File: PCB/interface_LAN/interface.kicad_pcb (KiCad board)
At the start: 4 copper layers, 100 x 75 mm, 167 parts, among them J1 24VAC, J10 LIMIT12, J11 POT, J12 RS485, J4 Power, J5 Control Signals, J6 HR913550A, J7 Sensor Feedback, J8 UART, J9 POT, Q1 8550, Q2 TIP127, Q3 MMBT5551, SW1 SW_SPST, SW2 CW, SW3 CCW, SW4 SET, U1 B1205-1W, U10 EL357, U11 74HCT595, U12 EL357, U13 AT24C64, U14 TL072, U15 HCNR201, U17 LMV358, U18 EL357, U19 EL357, U2 ESP32-WROOM-32, U20 EL357, U21 MAX485E, U22 TPS54160, U3 LM317_TO-220, U4 L78L05_SOT89, U5 AMS1117-3.3, U6 OLED_128x32_4pin, U7 LAN8720A, U9 HCNR201

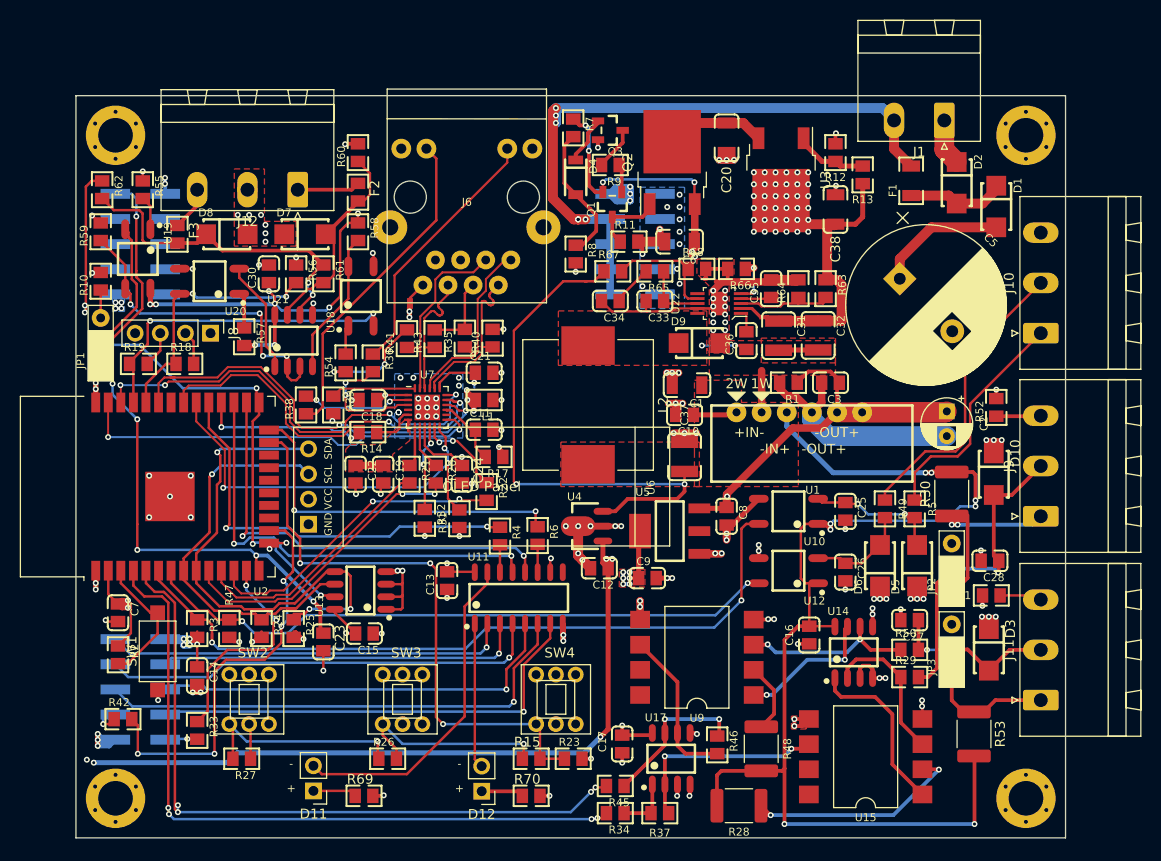
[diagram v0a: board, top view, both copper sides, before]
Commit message: Routed Interface_LAN MCU board
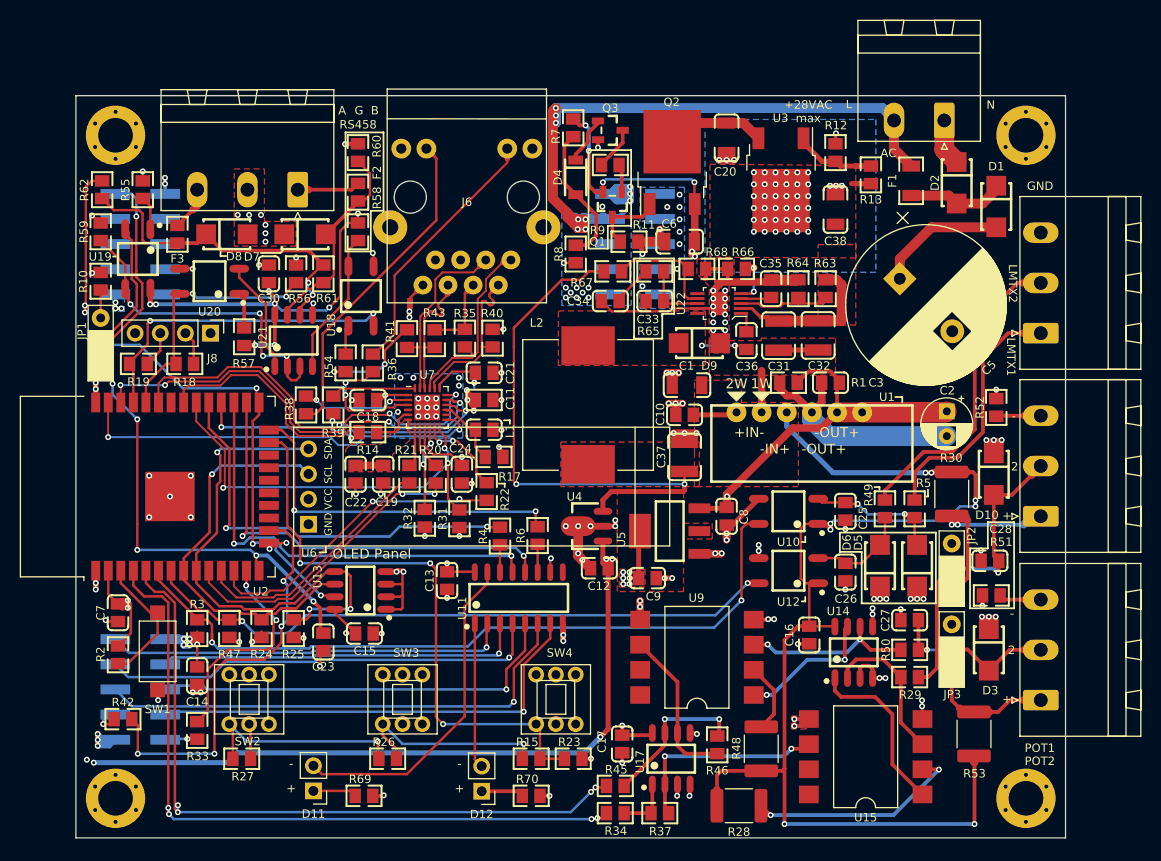
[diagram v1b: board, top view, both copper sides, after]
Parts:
- moved R13 0.83 mm to (100.3, 28.0)
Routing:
- net /+24V: track 31.4 -> 14.8 mm
- net GNDPWR: track 129.7 -> 134.8 mm, vias 86 -> 87
- net Net-(J11-Pad1): track 10.2 -> 14.8 mm
- net Net-(J9-Pad1): track 20.3 -> 23.1 mm
- net Net-(J10-Pad1): track 23.7 -> 25.7 mm
- net Net-(R12-Pad1): track 7.33 -> 8.92 mm
- net VAC: track 71.4 -> 72.9 mm, vias 6 -> 16
- net Net-(J10-Pad2): track 30.3 -> 31.6 mm
- net GND: track 104.7 -> 105.8 mm, vias 68 -> 66
- net /SDA: track 52.2 -> 52.8 mm
- net +12V: track 214.1 -> 214.7 mm
- added copper zone on B.Cu, net /+24V
- added copper zone on F.Cu, net /+24V
- added copper zone on B.Cu, net VAC
- added copper zone on In2.Cu, net VAC
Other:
- board text added: "+28VAC max"
- board text added: "2"
- board text added: "A"
- board text added: "AC"
- board text added: "B"
- board text added: "G"
- board text added: "GND"
- board text added: "L"
- board text added: "LMTX1"
- board text added: "LMTX2"
- board text added: "N"
- board text added: "POT1"
- board text added: "POT2"
- board text added: "RS458"

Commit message: Implemented the ESP-IDF version. First passed compilation
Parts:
- added C29: 104, lc_lib:0805_C, F.Cu at (62.1, 83.5)
- added C39: 104, lc_lib:0805_C, F.Cu at (70.2, 89.7)
- added C4: 1000uF 63V, Connector_JST:JST_XH_B2B-XH-A_1x02_P2.50mm_Vertical, F.Cu at (105.0, 40.3)
- added C40: 104, lc_lib:0805_C, F.Cu at (70.2, 92.5)
- added J2: 0, lc_lib:1206_R, F.Cu at (89.2, 26.2)
- added J3: JTAG, Connector_PinHeader_2.54mm:PinHeader_1x04_P2.54mm_Vertical, F.Cu at (48.8, 90.3)
- R3: value 4.7K -> 100K
- R9: value 47K -> 10K
- U7: footprint Package_DFN_QFN:QFN-24-1EP_4x4mm_P0.5mm_EP2.6x2.6mm -> lc_lib:QFN-24_4X4X05P
- moved R3 25.3 mm to (57.5, 73.8)
- moved R47 18.2 mm to (53.7, 74.4), turned to 180 degrees
- moved R69 9.71 mm to (44.0, 82.5), turned to 90 degrees
- moved C23 9.49 mm to (35.6, 73.9)
- turned U7 to 270 degrees
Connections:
- net /SPWM1 renamed /SPWM1_TCK
- net /SPWM2 renamed /SPWM2_TMS
- D11 pad 2: /LEDAX -> /LEDAX_485RW
- J8 pad 2: /PROG_TXD -> /PROG_RXD
- J8 pad 3: /PROG_RXD -> /PROG_TXD
- JP1 pad 2: /BOOT_WP_485RW -> /BOOT_WP
- R18 pad 2: /PROG_TXD -> /PROG_RXD
- R19 pad 2: /PROG_RXD -> /PROG_TXD
- R3 pad 1: /LMTX1 -> /LMTX2_TDO
- R3 pad 2: +3V3 -> GND
- R47 pad 2: /LMTX2 -> /LMTX2_TDO
- U10 pad 4: /LMTX1 -> /LMTX1_TDI
- U11 pad 15: /LEDAX -> /LEDAX_485RW
- U12 pad 4: /LMTX2 -> /LMTX2_TDO
- U13 pad 7: /BOOT_WP_485RW -> /BOOT_WP
- U19 pad 2: /BOOT_WP_485RW -> /LEDAX_485RW
- U2 pad 14: /ISense1 -> /LMTX1_TDI
- U2 pad 23: /ADC_Manual -> /LMTX2_TDO
- U2 pad 25: /BOOT_WP_485RW -> /BOOT_WP
- U2 pad 4: /POT1 -> /ISense1
- U2 pad 5: /POT2 -> /ADC_Manual
- U2 pad 6: /LMTX1 -> /POT1
- U2 pad 7: /LMTX2 -> /POT2
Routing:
- net /LEDAX_485RW: track 0.00 -> 107.3 mm, vias 0 -> 5
- net /LMTX2_TDO: track 0.00 -> 92.3 mm, vias 0 -> 5
- net /LMTX1_TDI: track 0.00 -> 78.9 mm, vias 0 -> 5
- net /LMTX1: track 76.9 -> 0.00 mm, vias 2 -> 0
- net /LMTX2: track 64.8 -> 0.00 mm, vias 2 -> 0
- net /BOOT_WP_485RW: track 58.1 -> 0.00 mm, vias 3 -> 0
- net /BOOT_WP: track 0.00 -> 44.6 mm, vias 0 -> 3
- net /LEDAX: track 33.6 -> 0.00 mm
- net /SPWM2_TMS: track 22.2 -> 55.4 mm, vias 2 -> 3
- net /SPWM1_TCK: track 41.9 -> 64.5 mm, vias 4 -> 5
- net +12V: track 214.7 -> 197.8 mm
- net /ISense1: track 65.6 -> 55.4 mm, vias 6 -> 5
- net VAC: track 72.9 -> 81.5 mm
- net /ADC_Manual: track 59.7 -> 65.4 mm, vias 3 -> 1
- net Net-(D11-Pad1): track 4.43 -> 7.85 mm
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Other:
- rule pad_to_mask_clearance: 0.051 -> 0.0508
- board text added: "* * *"
- board text added: "+3V3"
- board text added: "2P"
- board text added: "3P"
- board text added: "JP2"
- board text added: "JP3"
- board text added: "JTAG"
- board text added: "LEDA"
- board text added: "LEDB"
- board text added: "NOLOG"
- board text added: "POT Wiring"
- board text added: "PROG"
- board text added: "RST"
- board text added: "Rotator Interface May 18, 2022 By Lu, Zening (BI4WOP)"
- board text added: "Rx"
- board text added: "Solder to Bypass"
- board text added: "TCK"
- board text added: "TDI"
- board text added: "TDO"
- board text added: "TMS"
- board text added: "Tx"
- board text added: "V2.0"
